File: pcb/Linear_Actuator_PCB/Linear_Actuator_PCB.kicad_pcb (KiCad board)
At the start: 2 copper layers, 108.5 x 42.9 mm, 45 parts, among them J1 Pwr/Coms, J2 Pot, J3 Bootloader Pins, J5 LED, J7 8P8C, SW1 SW_Push, U1 ATmega328P-AU, Y1 Crystal

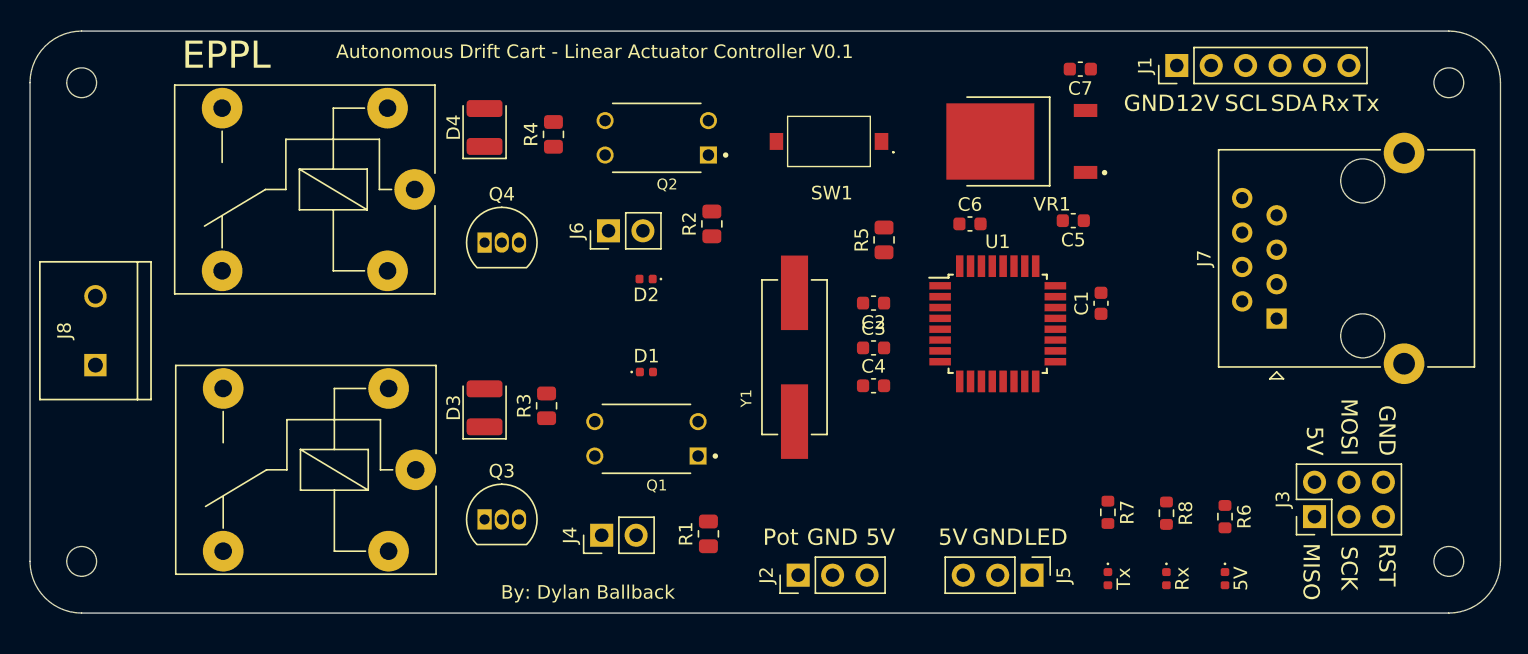
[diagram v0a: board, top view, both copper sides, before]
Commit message: Finished tracing the Linear Actuator
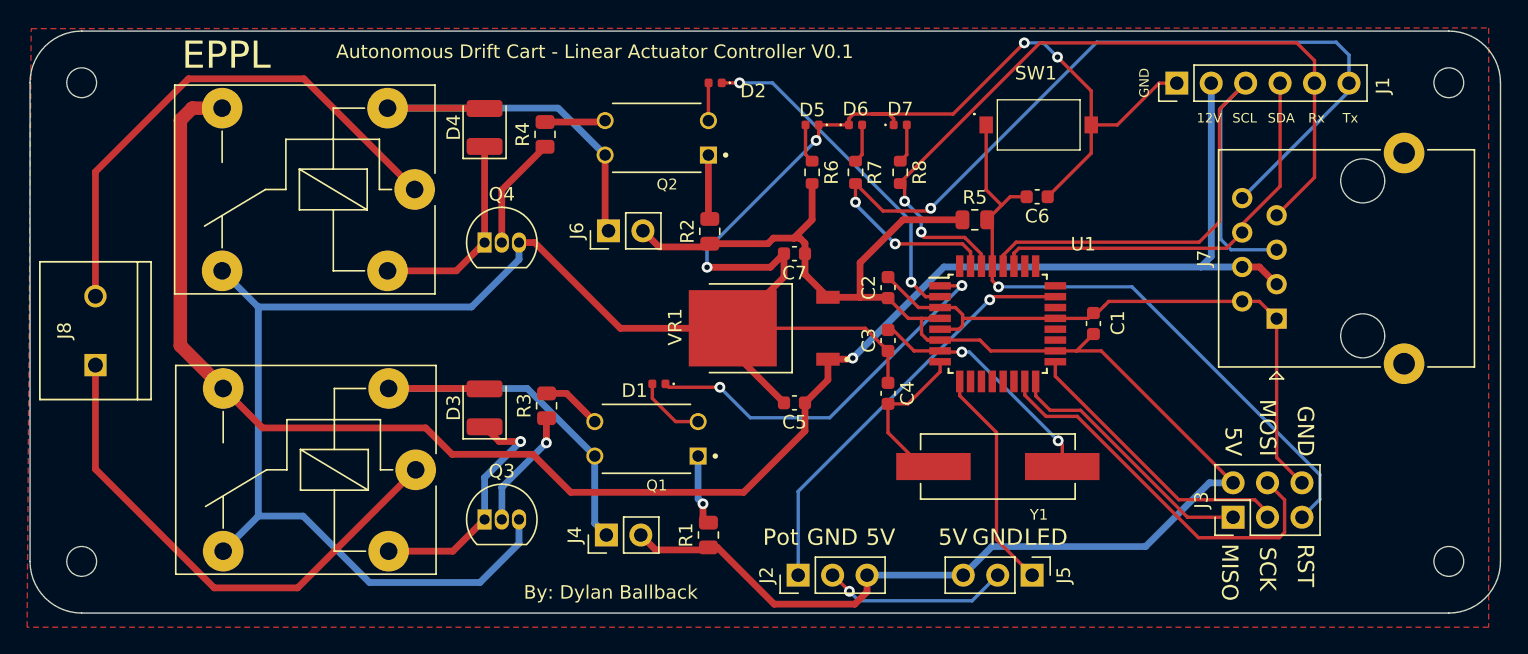
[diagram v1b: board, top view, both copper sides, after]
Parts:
- moved D5 45.2 mm to (157.0, 75.5), turned to 180 degrees
- moved R6 39.7 mm to (157.0, 79.0)
- moved D7 38.8 mm to (163.5, 75.5), turned to 0 degrees
- moved D6 38.3 mm to (160.2, 75.5), turned to 0 degrees
- moved R8 31.9 mm to (163.5, 79.0)
- moved R7 31.2 mm to (160.2, 79.0)
- moved C7 25.1 mm to (155.7, 85.0)
- moved C5 24.6 mm to (155.7, 96.0)
- moved VR1 23.5 mm to (153.5, 90.5)
- moved Y1 17.0 mm to (170.7, 100.7), turned to 180 degrees
- moved SW1 15.5 mm to (173.7, 75.5), turned to 0 degrees
- moved D2 15.3 mm to (149.8, 72.4)
- moved G*** 12.2 mm to (152.9, 89.8), turned to -135 degrees
- moved R5 6.86 mm to (169.0, 82.5), turned to 0 degrees
- moved J3 6.01 mm to (188.1, 104.4)
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- renumbered 5V to D5, Tx to D6, Rx to D7
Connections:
- D1 pad 1: /relay/Relay1 -> /Relay1
- D2 pad 1: /relay/Relay2 -> /Relay2
- U1 pad 1: /relay1 -> /Relay1
- U1 pad 2: /relay2 -> /Relay2
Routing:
- net GND: track 0.00 -> 239.3 mm, vias 0 -> 5
- net +12V: track 0.00 -> 128.8 mm, vias 0 -> 1
- net +5V: track 0.00 -> 123.3 mm
- net /TXD: track 0.00 -> 69.1 mm, vias 0 -> 3
- net /RXD: track 0.00 -> 58.3 mm, vias 0 -> 2
- net /Reset: track 0.00 -> 48.4 mm, vias 0 -> 1
- net /SCL: track 0.00 -> 45.5 mm
- net Motor+: track 0.00 -> 38.9 mm
- net Motor-: track 0.00 -> 38.5 mm
- net /pot: track 0.00 -> 31.1 mm, vias 0 -> 1
- net /SDA: track 0.00 -> 30.6 mm
- net Net-(D3-Pad2): track 0.00 -> 30.5 mm
- net Net-(D4-Pad2): track 0.00 -> 30.3 mm
- net /MOSI: track 0.00 -> 28.9 mm
- net /Relay1: track 0.00 -> 28.6 mm, vias 0 -> 2
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- added copper zone on F.Cu, net GND
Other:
- board text removed: "The placement of the LEDs doesn't matter too much it is what ever is easier for you."
- board text removed: "You can also slightly expand the spacing between all the componets if it makes the routing easier. The only imporant thing is the capacitors near the ATMega328p and the oscilator."
